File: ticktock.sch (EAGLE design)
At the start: 34 parts, among them IC1 ATMEGA644A, IC2 AD8611R, J1 AVR_SPI_PRG_6NS, Q1 MOSFET-NCHANNEL2N7002PW, U1 MAX232SOIC16, U2 OSCILLATORSMD, U3 FT232RLSSOP

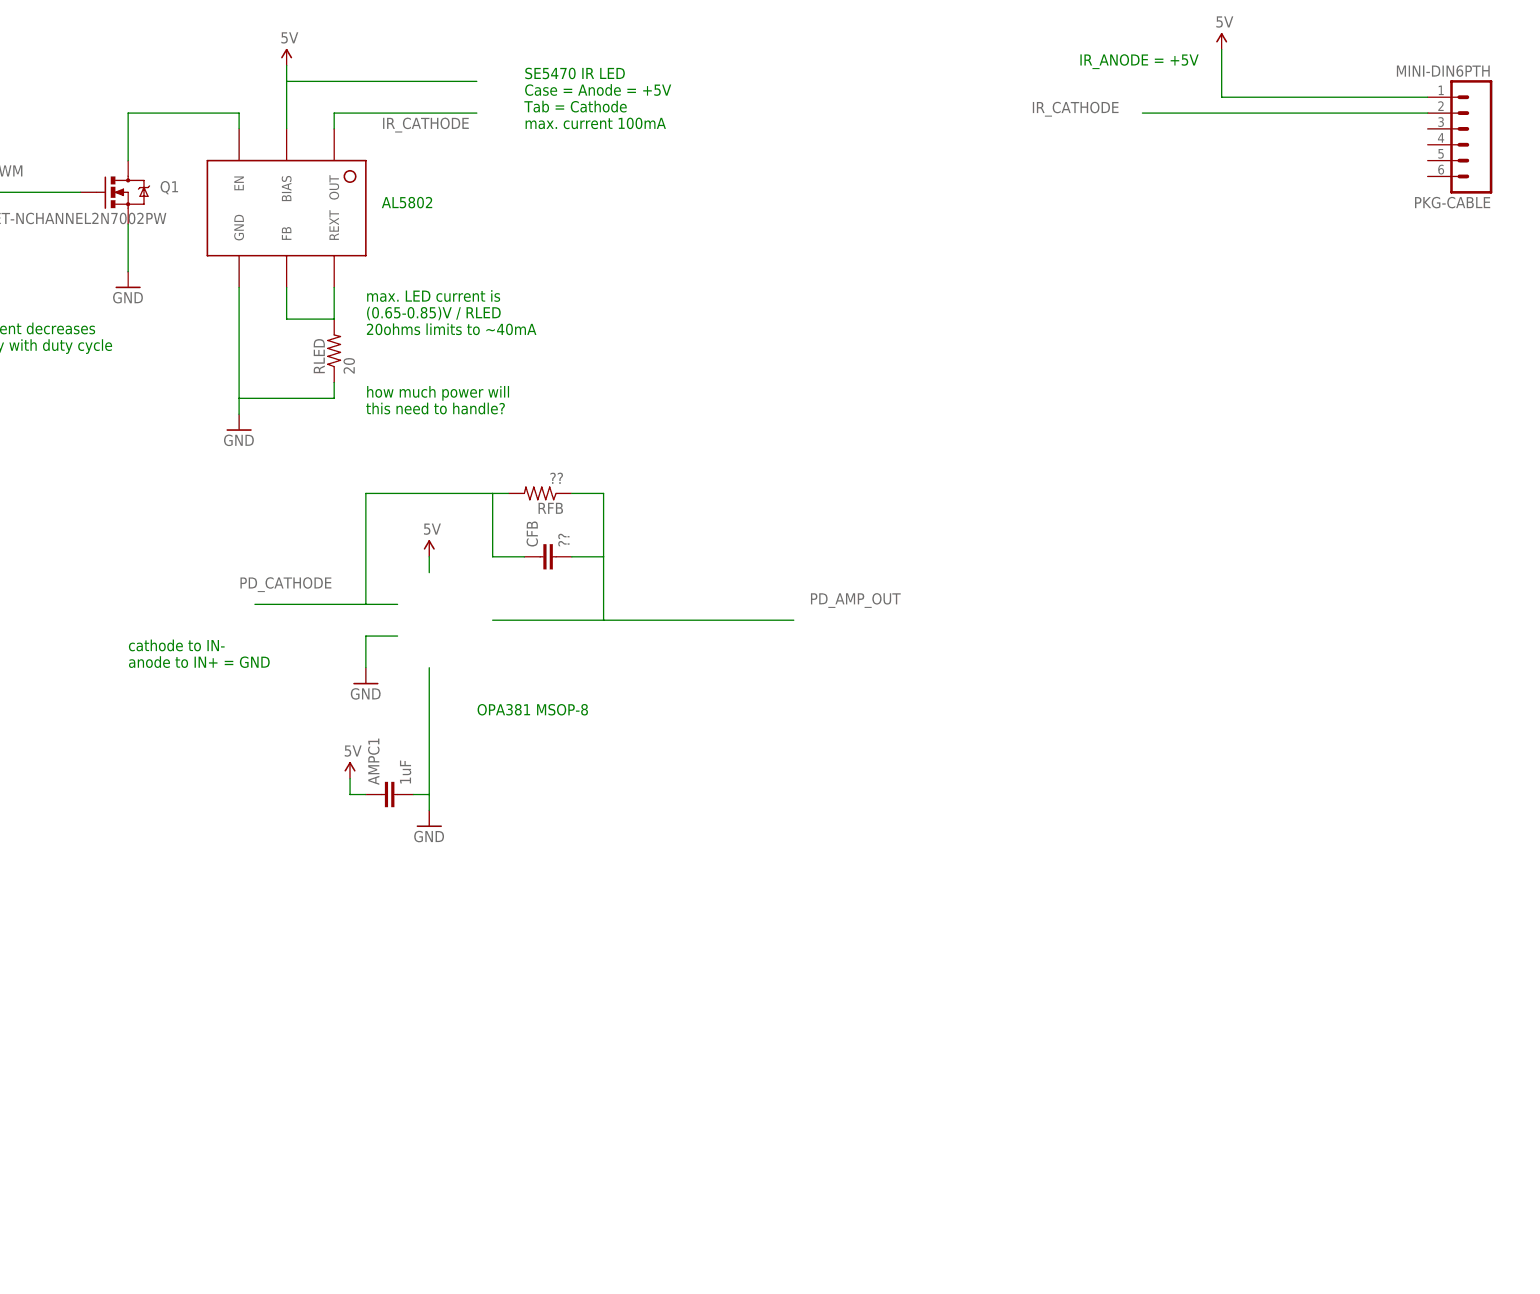
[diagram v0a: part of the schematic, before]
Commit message: Finish op-amp circuit
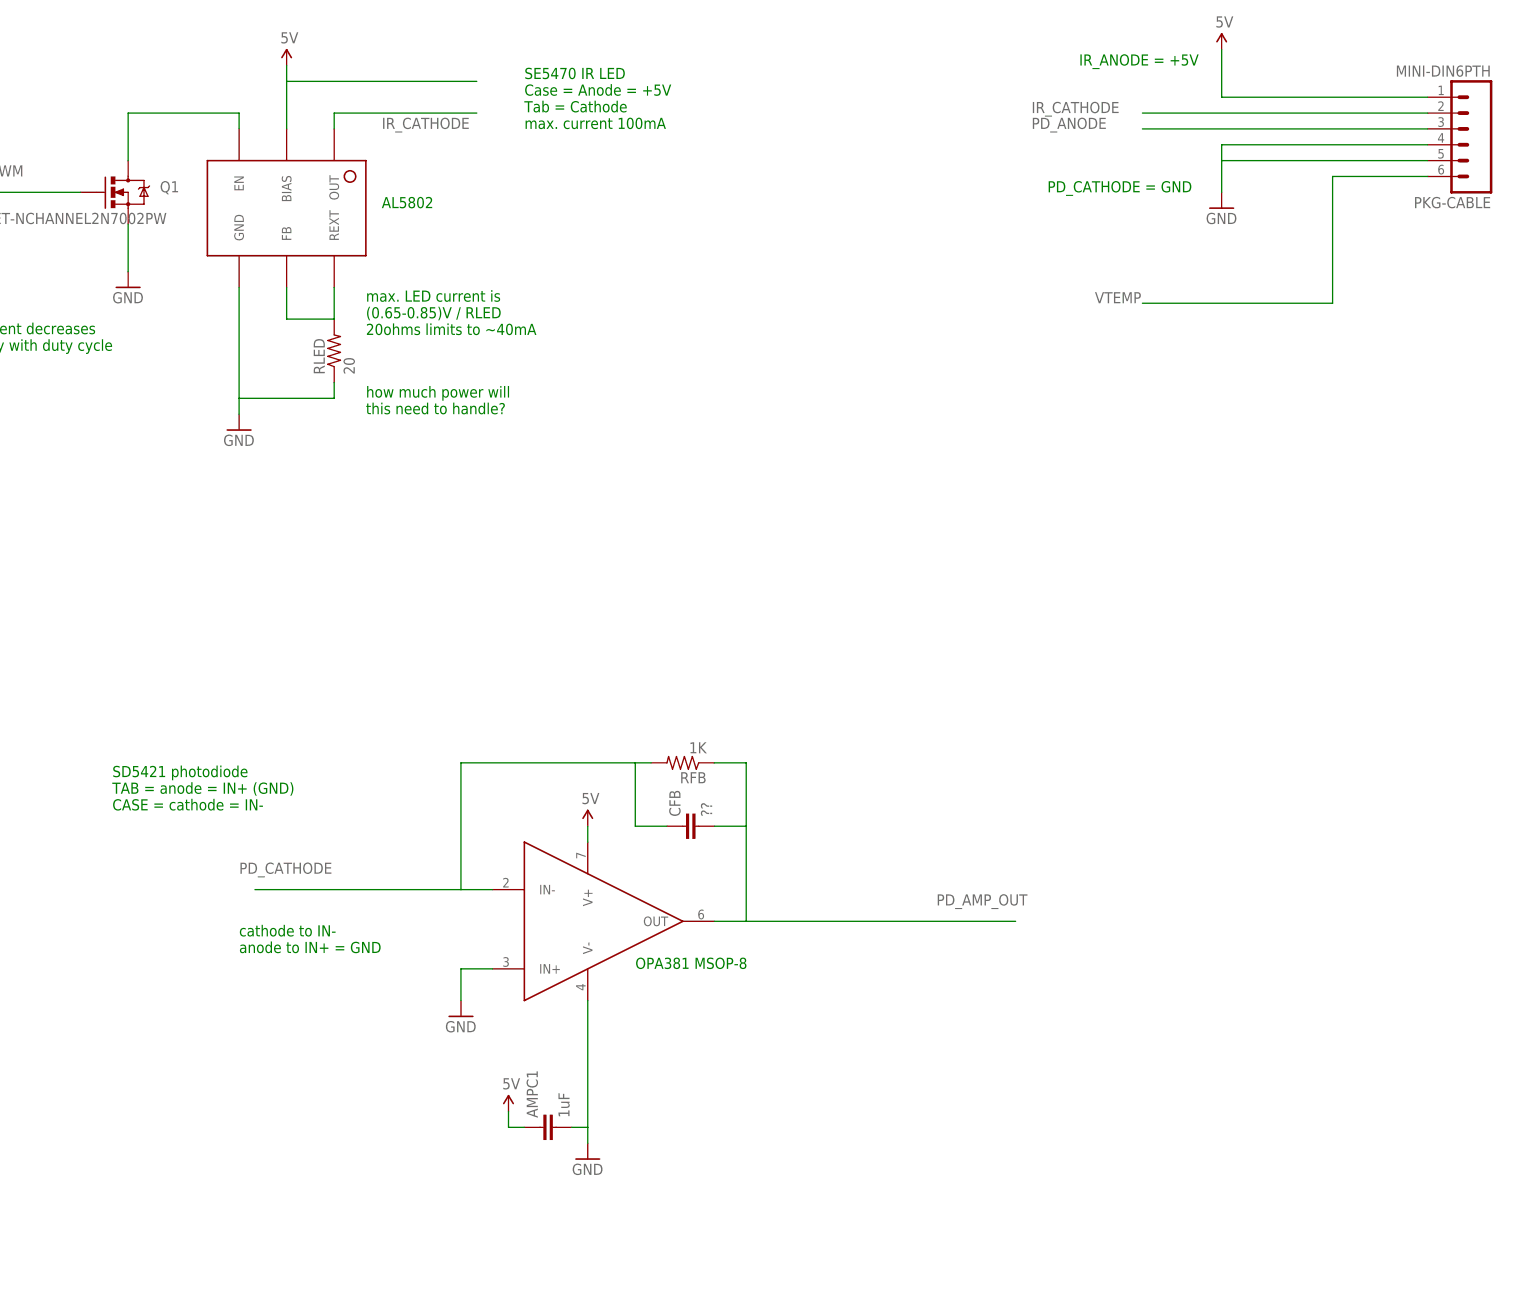
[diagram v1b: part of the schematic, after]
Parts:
- added U$1: (no value), tickTockLibrary:OPA381
- RFB: value ?? -> 1K
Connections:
- new net PD_ANODE: PKG-CABLE.3
- new net VTEMP: PKG-CABLE.6
- net GND: now also PKG-CABLE.4, PKG-CABLE.5
- net PD_CATHODE: now also U$1.IN-
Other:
- note added: "PD_CATHODE = GND"
- note added: "SD5421 photodiode TAB = anode = IN+ (GND) CASE = cathode = IN-"
- moved on the sheet: AMPC1, CFB, RFB
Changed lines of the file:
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@@
 <part name="SUPPLY17" library="SparkFun-Aesthetics" deviceset="5V" device=""/>
 <part name="SUPPLY18" library="SparkFun-Aesthetics" deviceset="5V" device=""/>
-<part name="RFB" library="SparkFun-Resistors" deviceset="RESISTOR" device="0805-RES" value="??"/>
+<part name="RFB" library="SparkFun-Resistors" deviceset="RESISTOR" device="0805-RES" value="1K"/>
 <part name="CFB" library="SparkFun-Capacitors" deviceset="CAP" device="0805" value="??"/>
 <part name="AMPC1" library="SparkFun-Capacitors" deviceset="CAP" device="0805" value="1uF"/>
 <part name="GND21" library="SparkFun-Aesthetics" deviceset="GND" device=""/>
+<part name="U$1" library="tickTockLibrary" deviceset="OPA381" device=""/>
+<part name="GND22" library="SparkFun-Aesthetics" deviceset="GND" device=""/>
 </parts>
 <sheets>
@@
 <text x="320.04" y="320.04" size="1.778" layer="91">1.1-1.8 Vpp into 50ohms
 sinusoidal</text>
-<text x="91.44" y="314.96" size="1.778" layer="91">OPA381 MSOP-8</text>
-<text x="35.56" y="322.58" size="1.778" layer="91">cathode to IN-
+<text x="116.84" y="274.32" size="1.778" layer="91">OPA381 MSOP-8</text>
+<text x="53.34" y="276.86" size="1.778" layer="91">cathode to IN-
 anode to IN+ = GND</text>
+<text x="33.02" y="299.72" size="1.778" layer="91">SD5421 photodiode
+TAB = anode = IN+ (GND)
+CASE = cathode = IN-</text>
+<text x="182.88" y="398.78" size="1.778" layer="91">PD_CATHODE = GND</text>
 </plain>
 <instances>
@@
 <instance part="GPR2" gate="G$1" x="330.2" y="259.08" rot="R270"/>
 <instance part="GND19" gate="1" x="330.2" y="246.38"/>
-<instance part="GND20" gate="1" x="83.82" y="297.18"/>
-<instance part="SUPPLY17" gate="G$1" x="83.82" y="340.36"/>
-<instance part="SUPPLY18" gate="G$1" x="71.12" y="304.8"/>
-<instance part="RFB" gate="G$1" x="101.6" y="350.52" rot="R180"/>
-<instance part="CFB" gate="G$1" x="104.14" y="340.36" smashed="yes" rot="R90">
-<attribute name="NAME" x="101.219" y="341.884" size="1.778" layer="95" rot="R90"/>
-<attribute name="VALUE" x="106.299" y="341.884" size="1.778" layer="96" rot="R90"/>
-</instance>
-<instance part="AMPC1" gate="G$1" x="78.74" y="302.26" smashed="yes" rot="R90">
-<attribute name="NAME" x="75.819" y="303.784" size="1.778" layer="95" rot="R90"/>
-<attribute name="VALUE" x="80.899" y="303.784" size="1.778" layer="96" rot="R90"/>
-</instance>
-<instance part="GND21" gate="1" x="73.66" y="320.04"/>
+<instance part="GND20" gate="1" x="109.22" y="243.84"/>
+<instance part="SUPPLY17" gate="G$1" x="109.22" y="297.18"/>
+<instance part="SUPPLY18" gate="G$1" x="96.52" y="251.46"/>
+<instance part="RFB" gate="G$1" x="124.46" y="307.34" rot="R180"/>
+<instance part="CFB" gate="G$1" x="127" y="297.18" smashed="yes" rot="R90">
+<attribute name="NAME" x="124.079" y="298.704" size="1.778" layer="95" rot="R90"/>
+<attribute name="VALUE" x="129.159" y="298.704" size="1.778" layer="96" rot="R90"/>
+</instance>
+<instance part="AMPC1" gate="G$1" x="104.14" y="248.92" smashed="yes" rot="R90">
+<attribute name="NAME" x="101.219" y="250.444" size="1.778" layer="95" rot="R90"/>
+<attribute name="VALUE" x="106.299" y="250.444" size="1.778" layer="96" rot="R90"/>
+</instance>
+<instance part="GND21" gate="1" x="88.9" y="266.7"/>
+<instance part="U$1" gate="G$1" x="109.22" y="281.94"/>
+<instance part="GND22" gate="1" x="210.82" y="396.24"/>
 </instances>
 <busses>
@@
 <segment>
 <pinref part="GND20" gate="1" pin="GND"/>
-<wire x1="83.82" y1="322.58" x2="83.82" y2="302.26" width="0.1524" layer="91"/>
+<wire x1="109.22" y1="269.24" x2="109.22" y2="248.92" width="0.1524" layer="91"/>
 <pinref part="AMPC1" gate="G$1" pin="2"/>
-<wire x1="83.82" y1="302.26" x2="83.82" y2="299.72" width="0.1524" layer="91"/>
-<wire x1="81.28" y1="302.26" x2="83.82" y2="302.26" width="0.1524" layer="91"/>
-</segment>
-<segment>
-<wire x1="78.74" y1="327.66" x2="73.66" y2="327.66" width="0.1524" layer="91"/>
-<wire x1="73.66" y1="327.66" x2="73.66" y2="322.58" width="0.1524" layer="91"/>
+<wire x1="109.22" y1="248.92" x2="109.22" y2="246.38" width="0.1524" layer="91"/>
+<wire x1="106.68" y1="248.92" x2="109.22" y2="248.92" width="0.1524" layer="91"/>
+</segment>
+<segment>
+<wire x1="93.98" y1="274.32" x2="88.9" y2="274.32" width="0.1524" layer="91"/>
+<wire x1="88.9" y1="274.32" x2="88.9" y2="269.24" width="0.1524" layer="91"/>
 <pinref part="GND21" gate="1" pin="GND"/>
+</segment>
+<segment>
+<pinref part="PKG-CABLE" gate="G$1" pin="4"/>
+<wire x1="243.84" y1="406.4" x2="210.82" y2="406.4" width="0.1524" layer="91"/>
+<wire x1="210.82" y1="406.4" x2="210.82" y2="403.86" width="0.1524" layer="91"/>
+<pinref part="GND22" gate="1" pin="GND"/>
+<pinref part="PKG-CABLE" gate="G$1" pin="5"/>
+<wire x1="210.82" y1="403.86" x2="210.82" y2="398.78" width="0.1524" layer="91"/>
+<wire x1="243.84" y1="403.86" x2="210.82" y2="403.86" width="0.1524" layer="91"/>
 </segment>
 </net>
@@
 <segment>
 <pinref part="SUPPLY17" gate="G$1" pin="5V"/>
-<wire x1="83.82" y1="340.36" x2="83.82" y2="337.82" width="0.1524" layer="91"/>
+<wire x1="109.22" y1="297.18" x2="109.22" y2="294.64" width="0.1524" layer="91"/>
 </segment>
 <segment>
 <pinref part="SUPPLY18" gate="G$1" pin="5V"/>
-<wire x1="71.12" y1="304.8" x2="71.12" y2="302.26" width="0.1524" layer="91"/>
+<wire x1="96.52" y1="251.46" x2="96.52" y2="248.92" width="0.1524" layer="91"/>
 <pinref part="AMPC1" gate="G$1" pin="1"/>
-<wire x1="71.12" y1="302.26" x2="73.66" y2="302.26" width="0.1524" layer="91"/>
+<wire x1="96.52" y1="248.92" x2="99.06" y2="248.92" width="0.1524" layer="91"/>
 </segment>
 </net>
@@
 <net name="PD_AMP_OUT" class="0">
 <segment>
-<wire x1="93.98" y1="330.2" x2="111.76" y2="330.2" width="0.1524" layer="91"/>
+<wire x1="129.54" y1="281.94" x2="134.62" y2="281.94" width="0.1524" layer="91"/>
+<label x="165.1" y="284.48" size="1.778" layer="95"/>
+<pinref part="RFB" gate="G$1" pin="1"/>
+<wire x1="134.62" y1="281.94" x2="177.8" y2="281.94" width="0.1524" layer="91"/>
+<wire x1="134.62" y1="307.34" x2="129.54" y2="307.34" width="0.1524" layer="91"/>
+<wire x1="134.62" y1="297.18" x2="134.62" y2="307.34" width="0.1524" layer="91"/>
 <pinref part="CFB" gate="G$1" pin="2"/>
-<wire x1="111.76" y1="330.2" x2="142.24" y2="330.2" width="0.1524" layer="91"/>
-<wire x1="106.68" y1="340.36" x2="111.76" y2="340.36" width="0.1524" layer="91"/>
-<wire x1="111.76" y1="340.36" x2="111.76" y2="330.2" width="0.1524" layer="91"/>
-<wire x1="111.76" y1="340.36" x2="111.76" y2="350.52" width="0.1524" layer="91"/>
-<pinref part="RFB" gate="G$1" pin="1"/>
-<wire x1="111.76" y1="350.52" x2="106.68" y2="350.52" width="0.1524" layer="91"/>
-<label x="144.78" y="332.74" size="1.778" layer="95"/>
+<wire x1="129.54" y1="297.18" x2="134.62" y2="297.18" width="0.1524" layer="91"/>
+<wire x1="134.62" y1="297.18" x2="134.62" y2="281.94" width="0.1524" layer="91"/>
 </segment>
 </net>
@@
 <segment>
 <pinref part="CFB" gate="G$1" pin="1"/>
-<wire x1="99.06" y1="340.36" x2="93.98" y2="340.36" width="0.1524" layer="91"/>
-<wire x1="93.98" y1="340.36" x2="93.98" y2="350.52" width="0.1524" layer="91"/>
+<wire x1="121.92" y1="297.18" x2="116.84" y2="297.18" width="0.1524" layer="91"/>
+<wire x1="116.84" y1="297.18" x2="116.84" y2="307.34" width="0.1524" layer="91"/>
 <pinref part="RFB" gate="G$1" pin="2"/>
-<wire x1="93.98" y1="350.52" x2="96.52" y2="350.52" width="0.1524" layer="91"/>
-<wire x1="93.98" y1="350.52" x2="73.66" y2="350.52" width="0.1524" layer="91"/>
-<wire x1="73.66" y1="350.52" x2="73.66" y2="332.74" width="0.1524" layer="91"/>
-<wire x1="73.66" y1="332.74" x2="78.74" y2="332.74" width="0.1524" layer="91"/>
-<wire x1="73.66" y1="332.74" x2="55.88" y2="332.74" width="0.1524" layer="91"/>
-<label x="53.34" y="335.28" size="1.778" layer="95"/>
-</segment>
-</net>
+<wire x1="116.84" y1="307.34" x2="119.38" y2="307.34" width="0.1524" layer="91"/>
+<wire x1="116.84" y1="307.34" x2="88.9" y2="307.34" width="0.1524" layer="91"/>
+<wire x1="88.9" y1="307.34" x2="88.9" y2="287.02" width="0.1524" layer="91"/>
+<pinref part="U$1" gate="G$1" pin="IN-"/>
+<wire x1="88.9" y1="287.02" x2="93.98" y2="287.02" width="0.1524" layer="91"/>
+<wire x1="88.9" y1="287.02" x2="55.88" y2="287.02" width="0.1524" layer="91"/>
+<label x="53.34" y="289.56" size="1.778" layer="95"/>
+</segment>
+</net>
+<net name="PD_ANODE" class="0">
+<segment>
+<pinref part="PKG-CABLE" gate="G$1" pin="3"/>
+<wire x1="243.84" y1="408.94" x2="198.12" y2="408.94" width="0.1524" layer="91"/>
+<label x="180.34" y="408.94" size="1.778" layer="95"/>
+</segment>
+</net>
+<net name="VTEMP" class="0">
+<segment>
+<pinref part="PKG-CABLE" gate="G$1" pin="6"/>
+<wire x1="243.84" y1="401.32" x2="228.6" y2="401.32" width="0.1524" layer="91"/>
+<wire x1="228.6" y1="401.32" x2="228.6" y2="381" width="0.1524" layer="91"/>
+<wire x1="228.6" y1="381" x2="198.12" y2="381" width="0.1524" layer="91"/>
+<label x="190.5" y="381" size="1.778" layer="95"/>
+</segment>
+</net>
